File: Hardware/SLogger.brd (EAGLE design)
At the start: 22 x 33.5 mm, 16 parts, among them U2 DSPIC33FJ802GP-28, U7 USD-SOCKETNEW

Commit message: Finished 1.0 version of the new SLogger hardware.
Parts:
- added JP1: M03PTH, ASL:1X03
- added U4: MCP2551, SparkFun:SO08
- moved C9 13.0 mm to (20.8, 14.0), turned to 270 degrees
- moved R3 8.64 mm to (19.6, 1.52)
- moved C8 7.47 mm to (18.8, 7.11)
- moved R2 6.86 mm to (1.52, 2.54), turned to 90 degrees
- moved C1 6.18 mm to (2.54, 19.6), turned to 180 degrees
- moved C6 4.67 mm to (2.54, 21.3), turned to 180 degrees
- moved U1 4.58 mm to (6.35, 21.6)
- moved JP4 4.44 mm to (3.05, 17.3)
- moved J1 4.32 mm to (4.06, 25.7)
- moved JP2 4.32 mm to (9.65, 25.7)
- moved JP3 4.32 mm to (17.8, 25.7)
- moved U2 4.32 mm to (11.4, 9.65)
- moved C10 4.32 mm to (4.57, 6.35)
- moved LED2 2.87 mm to (20.4, 3.81), turned to 90 degrees
- moved LED1 1.61 mm to (1.52, 5.33), turned to 90 degrees
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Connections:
- new net CAN_HI: JP1.3, U4.7
- new net CAN_LO: JP1.2, U4.6
- new net CAN_RX: U2.P$25, U4.4
- new net CAN_TX: U2.P$7, U4.1
- new net VCC5V0: U4.3
- net GND: now also JP1.1, U4.2, U4.8
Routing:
- net GND: track 0.00 -> 120.1 mm, vias 0 -> 3
- net VCC3V3: track 0.00 -> 51.8 mm, vias 0 -> 3
- net UART2_TX: track 0.00 -> 20.6 mm, vias 0 -> 1
- net UART1_RX: track 0.00 -> 20.4 mm, vias 0 -> 1
- net UART1_TX: track 0.00 -> 20.0 mm, vias 0 -> 1
- net UART2_RX: track 0.00 -> 17.2 mm, vias 0 -> 1
- net CAN_TX: track 0.00 -> 16.9 mm, vias 0 -> 2
- net VCC: track 0.00 -> 9.54 mm
- net CAN_RX: track 0.00 -> 9.09 mm
- net CD: track 0.00 -> 8.91 mm, vias 0 -> 1
- net SDO: track 0.00 -> 7.32 mm, vias 0 -> 1
- net CS: track 0.00 -> 6.93 mm, vias 0 -> 1
- net SCK: track 0.00 -> 6.34 mm, vias 0 -> 1
- net PGC: track 0.00 -> 6.23 mm
- net LED1: track 0.00 -> 5.40 mm
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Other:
- board size 22 x 33.5 mm -> 22 x 29.2 mm

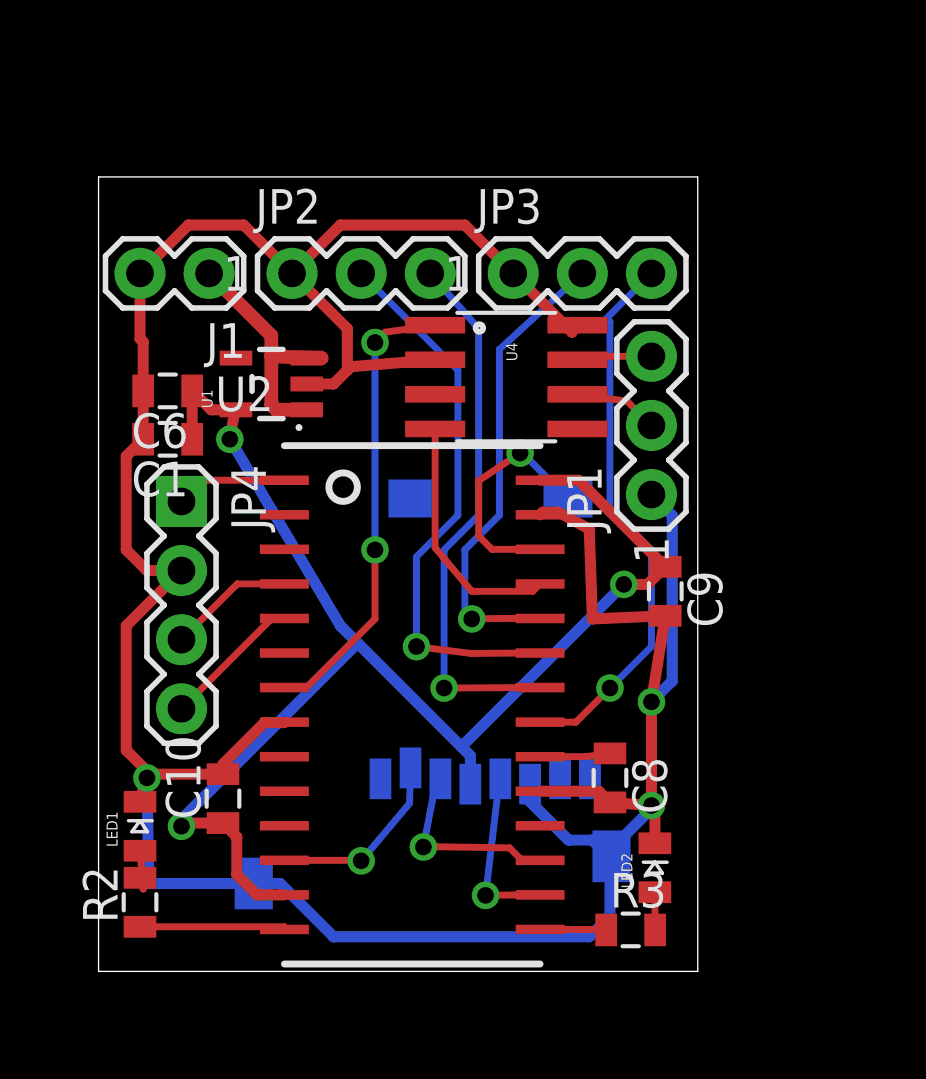
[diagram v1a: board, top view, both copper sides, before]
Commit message: Added marcellos changes and documented.
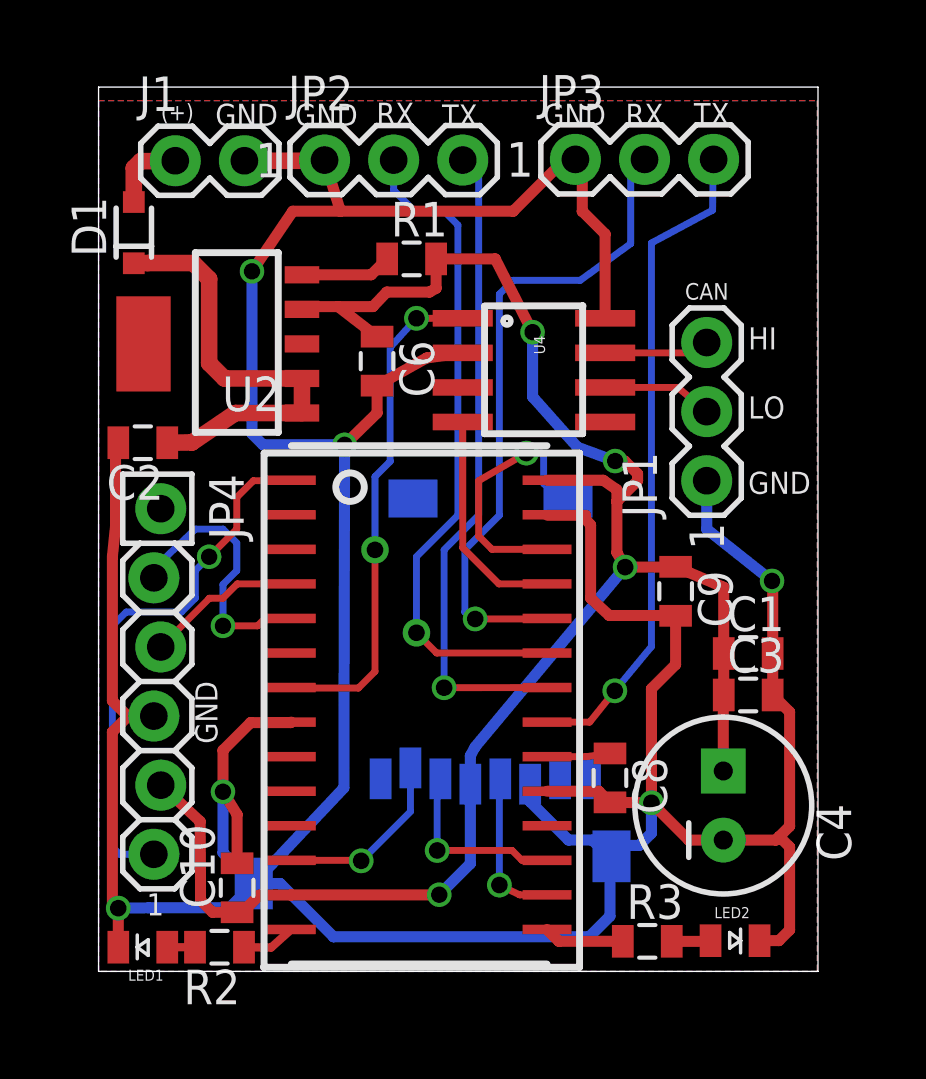
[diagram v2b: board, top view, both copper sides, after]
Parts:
- removed U1: (no value), SparkFun-PowerIC:SOT23-5
- added C2, C3: 4.7uF, ASL:0805
- added C4: (no value), ASL:CPOL-RADIAL-100UF-25V
- added D1: (no value), ASL:SOD-323F
- added R1: 100K, CMPE118lib:0805
- added U$2: MCP1826, ASL:SOT223-5
- C1: value .1uF -> 4.7uF
- JP4: device SparkFun-Connectors:1X04 -> ASL:1X06_LOCK
- moved C1 22.7 mm to (23.9, 11.7), turned to 0 degrees
- moved C6 7.77 mm to (10.2, 22.4), turned to 270 degrees
- moved JP3 4.77 mm to (20.1, 29.8)
- moved LED1 4.45 mm to (1.63, 0.89), turned to 180 degrees
- moved JP2 4.33 mm to (10.8, 29.8)
- moved J1 4.32 mm to (2.82, 29.8), turned to 0 degrees
- moved LED2 3.98 mm to (23.4, 1.13), turned to 0 degrees
- moved R2 3.36 mm to (4.45, 0.89), turned to 180 degrees
- moved C10 3.32 mm to (5.09, 3.07)
- moved JP1 2.09 mm to (22.4, 20.6)
- moved U4 1.05 mm to (16.0, 22.1)
- moved JP4 0.93 mm to (2.16, 17.0)
- moved R3 0.74 mm to (20.2, 1.10)
- moved C9 0.38 mm to (21.2, 14.0)
- moved U2 0.25 mm to (11.7, 9.65)
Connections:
- new net GND@3: U$2.P$3
- new net GND@6: U$2.P$6
- new net N$11: JP4.1
- new net N$2: D1.2, J1.1
- new net N$4: R1.1, U$2.P$5
- net GND: now also C2.2, C3.2, C4.2, JP4.4; no longer JP4.2, U1.2
- net MCLR: now also JP4.6; no longer JP4.1
- net PGC: now also JP4.2; no longer JP4.4
- net VCC: now also C2.1, D1.1, U$2.P$1, U$2.P$2; no longer J1.1, U1.1, U1.3
- net VCC3V3: now also C3.1, C4.1, JP4.5, R1.2, U$2.P$4; no longer U1.5
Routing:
- net GND: track 120.1 -> 163.2 mm, vias 3 -> 6
- net MCLR: track 4.54 -> 19.8 mm, vias 0 -> 1
- net VCC3V3: track 51.8 -> 67.0 mm, vias 3 -> 4
- net UART2_RX: track 17.2 -> 24.1 mm
- net VCC: track 9.54 -> 16.3 mm
- net PGC: track 6.23 -> 10.6 mm, vias 0 -> 1
- net UART1_RX: track 20.4 -> 24.7 mm
- net UART1_TX: track 20.0 -> 23.9 mm
- net UART2_TX: track 20.6 -> 24.4 mm
- net LED1: track 5.40 -> 1.99 mm
- net N$4: track 0.00 -> 3.37 mm
- net N$2: track 0.00 -> 2.88 mm
- net CAN_TX: track 16.9 -> 19.1 mm
- net PGD: track 4.63 -> 5.77 mm
- net CAN_HI: track 2.74 -> 3.83 mm
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- added copper zone on layer 1, net GND
- added copper zone on layer 16, net GND
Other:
- board size 22 x 29.2 mm -> 26.4 x 32.5 mm
- board text added: "(+)"
- board text added: "1"
- board text added: "CAN"
- board text added: "GND"
- board text added: "HI"
- board text added: "LO"
- board text added: "RX"
- board text added: "TX"
